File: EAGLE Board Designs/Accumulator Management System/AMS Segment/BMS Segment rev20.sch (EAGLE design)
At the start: 159 parts, among them J1 CONNECTOR-2_MICROFIT_SMD_RIGH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, J10 CONNECTOR-2_MICROFIT_SMD_RIGH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, J100 CONNECTOR-1_5222_, J101 CONNECTOR-1_5222_, J102 CONNECTOR-1_5222_, J103 CONNECTOR-1_5222_, J104 CONNECTOR-1_5222_, J105 CONNECTOR-1_5222_, J106 CONNECTOR-1_5222_, J107 CONNECTOR-1_5222_, J108 CONNECTOR-1_5222_, J109 CONNECTOR-1_5222_, J11 CONNECTOR-2_MICROFIT_SMD_RIGH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, J110 CONNECTOR-1_5222_, J111 CONNECTOR-1_5222_, J112 CONNECTOR-1_5222_, J113 CONNECTOR-1_5222_, J114 CONNECTOR-1_5222_, J115 CONNECTOR-1_5222_, J116 CONNECTOR-1_5222_, J117 CONNECTOR-1_5222_, J118 CONNECTOR-1_5222_, J119 CONNECTOR-1_5222_, J12 CONNECTOR-2_MICROFIT_SMD_RIGH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, J120 CONNECTOR-1_5222_, J121 CONNECTOR-1_5222_, J2 CONNECTOR-2_MICROFIT_SMD_RIGH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, J3 CONNECTOR-2_MICROFIT_SMD_RIGH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, J4 CONNECTOR-2_MICROFIT_SMD_RIGH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, J6 CONNECTOR-2_MICROFIT_SMD_RIGH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, J8 CONNECTOR-2_MICROFIT_SMD_RIGH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, J9 CONNECTOR-2_MICROFIT_SMD_RIGH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, T2 TRANSFORMER_HM2112ZNLT, U1 SHT31-ARP-B, U2 LTC6811-1, U3 LT3990-5, U4 LT3990-5, U5 LTC6811-1, U6 SHT31-ARP-B

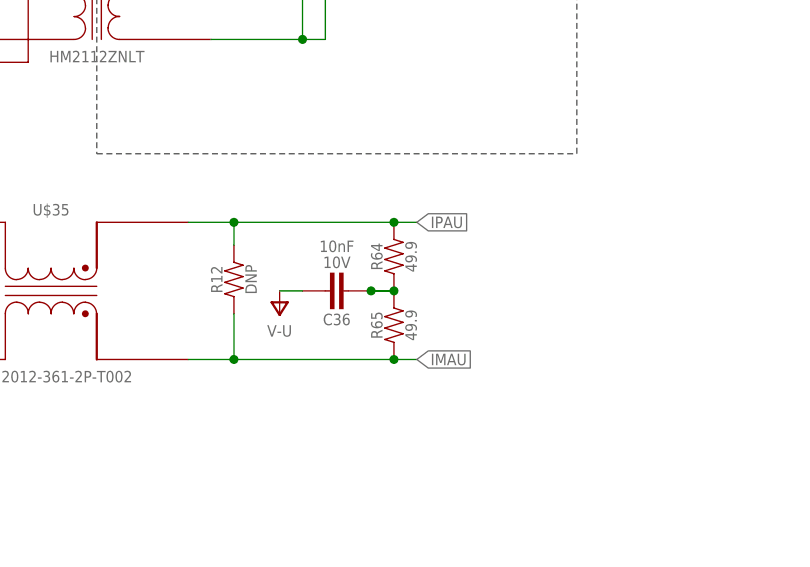
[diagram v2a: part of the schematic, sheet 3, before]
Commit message: Added Coupling Capacitors
Added Coupling Capacitors for isolation and to filter out DC noise in series for on-board chip-to-chip connection.
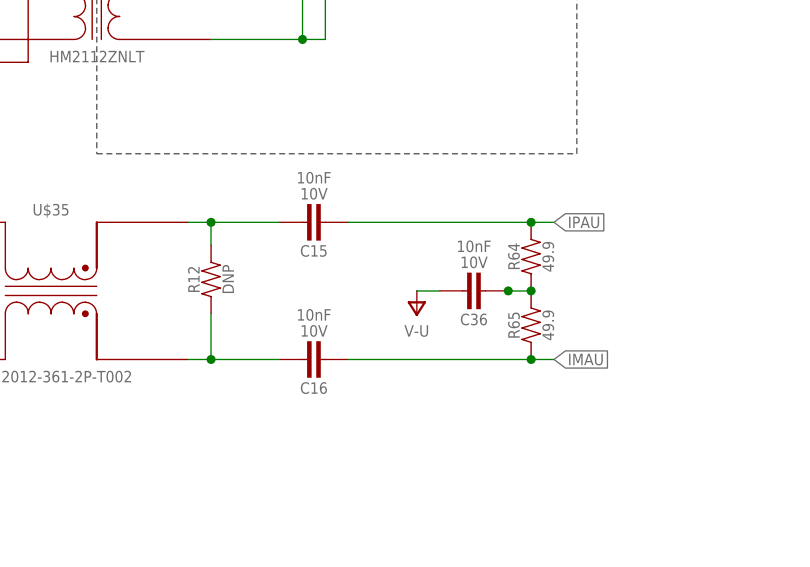
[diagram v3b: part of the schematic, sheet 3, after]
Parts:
- added C15, C16: CAPACITOR_0603_10V_10NF, HyTechDevices:CAPACITOR_0603_10V_10NF
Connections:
- net IMAU: now also C16.1, C16.2
- net IPAU: now also C15.1, C15.2
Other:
- moved on the sheet: C36, R12, R64, R65
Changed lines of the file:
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@@
 <part name="R11" library="HyTechDevices" deviceset="RESISTOR_?_*" device="0603" technology="DNP" value="RESISTOR_0603_DNP"/>
 <part name="R12" library="HyTechDevices" deviceset="RESISTOR_?_*" device="0603" technology="DNP" value="RESISTOR_0603_DNP"/>
+<part name="C15" library="HyTechDevices" deviceset="CAPACITOR_?_*" device="0603" technology="10V_10NF"/>
+<part name="C16" library="HyTechDevices" deviceset="CAPACITOR_?_*" device="0603" technology="10V_10NF"/>
 </parts>
 <sheets>
@@
 <attribute name="CAPACITANCE" x="71.882" y="138.43" size="1.27" layer="96" rot="R270" align="top-center"/>
 </instance>
-<instance part="R64" gate="G$1" x="137.16" y="83.82" smashed="yes" rot="R90">
-<attribute name="NAME" x="135.89" y="82.55" size="1.27" layer="95" rot="R90" align="bottom-center"/>
-<attribute name="RESISTANCE" x="138.43" y="82.55" size="1.27" layer="96" rot="R90" align="top-center"/>
-</instance>
-<instance part="R65" gate="G$1" x="137.16" y="76.2" smashed="yes" rot="R90">
-<attribute name="NAME" x="135.89" y="74.93" size="1.27" layer="95" rot="R90" align="bottom-center"/>
-<attribute name="RESISTANCE" x="138.43" y="74.93" size="1.27" layer="96" rot="R90" align="top-center"/>
-</instance>
-<instance part="C36" gate="G$1" x="129.54" y="78.74" smashed="yes" rot="R180">
-<attribute name="NAME" x="130.81" y="76.2" size="1.27" layer="95" rot="R180" align="bottom-center"/>
-<attribute name="VOLTAGE" x="130.81" y="81.28" size="1.27" layer="96" rot="R180" align="top-center"/>
-<attribute name="CAPACITANCE" x="130.81" y="83.058" size="1.27" layer="96" rot="R180" align="top-center"/>
+<instance part="R64" gate="G$1" x="152.4" y="83.82" smashed="yes" rot="R90">
+<attribute name="NAME" x="151.13" y="82.55" size="1.27" layer="95" rot="R90" align="bottom-center"/>
+<attribute name="RESISTANCE" x="153.67" y="82.55" size="1.27" layer="96" rot="R90" align="top-center"/>
+</instance>
+<instance part="R65" gate="G$1" x="152.4" y="76.2" smashed="yes" rot="R90">
+<attribute name="NAME" x="151.13" y="74.93" size="1.27" layer="95" rot="R90" align="bottom-center"/>
+<attribute name="RESISTANCE" x="153.67" y="74.93" size="1.27" layer="96" rot="R90" align="top-center"/>
+</instance>
+<instance part="C36" gate="G$1" x="144.78" y="78.74" smashed="yes" rot="R180">
+<attribute name="NAME" x="146.05" y="76.2" size="1.27" layer="95" rot="R180" align="bottom-center"/>
+<attribute name="VOLTAGE" x="146.05" y="81.28" size="1.27" layer="96" rot="R180" align="top-center"/>
+<attribute name="CAPACITANCE" x="146.05" y="83.058" size="1.27" layer="96" rot="R180" align="top-center"/>
 </instance>
 <instance part="P100" gate="G$1" x="81.28" y="132.08" smashed="yes">
 <attribute name="VALUE" x="81.28" y="130.81" size="1.27" layer="96" align="top-center"/>
 </instance>
-<instance part="P101" gate="G$1" x="124.46" y="76.2" smashed="yes">
-<attribute name="VALUE" x="124.46" y="74.93" size="1.27" layer="96" align="top-center"/>
+<instance part="P101" gate="G$1" x="139.7" y="76.2" smashed="yes">
+<attribute name="VALUE" x="139.7" y="74.93" size="1.27" layer="96" align="top-center"/>
 </instance>
 <instance part="R69" gate="G$1" x="127" y="119.38" smashed="yes" rot="R90">
@@
 <attribute name="RESISTANCE" x="82.55" y="80.01" size="1.27" layer="96" rot="R90" align="top-center"/>
 </instance>
-<instance part="R12" gate="G$1" x="119.38" y="81.28" smashed="yes" rot="R90">
-<attribute name="NAME" x="118.11" y="80.01" size="1.27" layer="95" rot="R90" align="bottom-center"/>
-<attribute name="RESISTANCE" x="120.65" y="80.01" size="1.27" layer="96" rot="R90" align="top-center"/>
+<instance part="R12" gate="G$1" x="116.84" y="81.28" smashed="yes" rot="R90">
+<attribute name="NAME" x="115.57" y="80.01" size="1.27" layer="95" rot="R90" align="bottom-center"/>
+<attribute name="RESISTANCE" x="118.11" y="80.01" size="1.27" layer="96" rot="R90" align="top-center"/>
+</instance>
+<instance part="C15" gate="G$1" x="127" y="86.36" smashed="yes" rot="R180">
+<attribute name="NAME" x="128.27" y="83.82" size="1.27" layer="95" rot="R180" align="bottom-center"/>
+<attribute name="VOLTAGE" x="128.27" y="88.9" size="1.27" layer="96" rot="R180" align="top-center"/>
+<attribute name="CAPACITANCE" x="128.27" y="90.678" size="1.27" layer="96" rot="R180" align="top-center"/>
+</instance>
+<instance part="C16" gate="G$1" x="127" y="71.12" smashed="yes" rot="R180">
+<attribute name="NAME" x="128.27" y="68.58" size="1.27" layer="95" rot="R180" align="bottom-center"/>
+<attribute name="VOLTAGE" x="128.27" y="73.66" size="1.27" layer="96" rot="R180" align="top-center"/>
+<attribute name="CAPACITANCE" x="128.27" y="75.438" size="1.27" layer="96" rot="R180" align="top-center"/>
 </instance>
 </instances>
@@
 <net name="IMAU" class="5">
 <segment>
-<pinref part="R65" gate="G$1" pin="1"/>
-<wire x1="137.16" y1="71.12" x2="139.7" y2="71.12" width="0.1524" layer="91"/>
-<label x="139.7" y="71.12" size="1.27" layer="95" xref="yes"/>
 <pinref part="U$35" gate="G$1" pin="3"/>
-<wire x1="137.16" y1="71.12" x2="119.38" y2="71.12" width="0.1524" layer="91"/>
-<junction x="137.16" y="71.12"/>
 <pinref part="R12" gate="G$1" pin="1"/>
-<wire x1="119.38" y1="71.12" x2="114.3" y2="71.12" width="0.1524" layer="91"/>
-<wire x1="119.38" y1="76.2" x2="119.38" y2="71.12" width="0.1524" layer="91"/>
-<junction x="119.38" y="71.12"/>
+<wire x1="116.84" y1="71.12" x2="114.3" y2="71.12" width="0.1524" layer="91"/>
+<wire x1="116.84" y1="76.2" x2="116.84" y2="71.12" width="0.1524" layer="91"/>
+<pinref part="C16" gate="G$1" pin="1"/>
+<wire x1="124.46" y1="71.12" x2="116.84" y2="71.12" width="0.1524" layer="91"/>
+<junction x="116.84" y="71.12"/>
+</segment>
+<segment>
+<pinref part="R65" gate="G$1" pin="1"/>
+<wire x1="152.4" y1="71.12" x2="154.94" y2="71.12" width="0.1524" layer="91"/>
+<label x="154.94" y="71.12" size="1.27" layer="95" xref="yes"/>
+<pinref part="C16" gate="G$1" pin="2"/>
+<wire x1="152.4" y1="71.12" x2="132.08" y2="71.12" width="0.1524" layer="91"/>
+<junction x="152.4" y="71.12"/>
 </segment>
 </net>
 <net name="IPAU" class="5">
 <segment>
-<pinref part="R64" gate="G$1" pin="2"/>
-<wire x1="137.16" y1="86.36" x2="139.7" y2="86.36" width="0.1524" layer="91"/>
-<label x="139.7" y="86.36" size="1.27" layer="95" xref="yes"/>
 <pinref part="U$35" gate="G$1" pin="4"/>
-<wire x1="137.16" y1="86.36" x2="119.38" y2="86.36" width="0.1524" layer="91"/>
-<junction x="137.16" y="86.36"/>
 <pinref part="R12" gate="G$1" pin="2"/>
-<wire x1="119.38" y1="86.36" x2="114.3" y2="86.36" width="0.1524" layer="91"/>
-<wire x1="119.38" y1="83.82" x2="119.38" y2="86.36" width="0.1524" layer="91"/>
-<junction x="119.38" y="86.36"/>
+<wire x1="116.84" y1="86.36" x2="114.3" y2="86.36" width="0.1524" layer="91"/>
+<wire x1="116.84" y1="83.82" x2="116.84" y2="86.36" width="0.1524" layer="91"/>
+<pinref part="C15" gate="G$1" pin="1"/>
+<wire x1="124.46" y1="86.36" x2="116.84" y2="86.36" width="0.1524" layer="91"/>
+<junction x="116.84" y="86.36"/>
+</segment>
+<segment>
+<pinref part="R64" gate="G$1" pin="2"/>
+<wire x1="152.4" y1="86.36" x2="154.94" y2="86.36" width="0.1524" layer="91"/>
+<label x="154.94" y="86.36" size="1.27" layer="95" xref="yes"/>
+<pinref part="C15" gate="G$1" pin="2"/>
+<wire x1="152.4" y1="86.36" x2="132.08" y2="86.36" width="0.1524" layer="91"/>
+<junction x="152.4" y="86.36"/>
 </segment>
 </net>
@@
 <pinref part="R65" gate="G$1" pin="2"/>
 <pinref part="C36" gate="G$1" pin="2"/>
-<wire x1="134.62" y1="78.74" x2="137.16" y2="78.74" width="0.1524" layer="91"/>
-<junction x="137.16" y="78.74"/>
-<wire x1="134.62" y1="78.74" x2="137.16" y2="78.74" width="0.1524" layer="91"/>
-<junction x="134.62" y="78.74"/>
+<junction x="152.4" y="78.74"/>
+<wire x1="149.86" y1="78.74" x2="152.4" y2="78.74" width="0.1524" layer="91"/>
+<junction x="149.86" y="78.74"/>
 </segment>
 </net>
@@
 <segment>
 <pinref part="C36" gate="G$1" pin="1"/>
-<wire x1="127" y1="78.74" x2="124.46" y2="78.74" width="0.1524" layer="91"/>
+<wire x1="142.24" y1="78.74" x2="139.7" y2="78.74" width="0.1524" layer="91"/>
 <pinref part="P101" gate="G$1" pin="V-U"/>
 </segment>

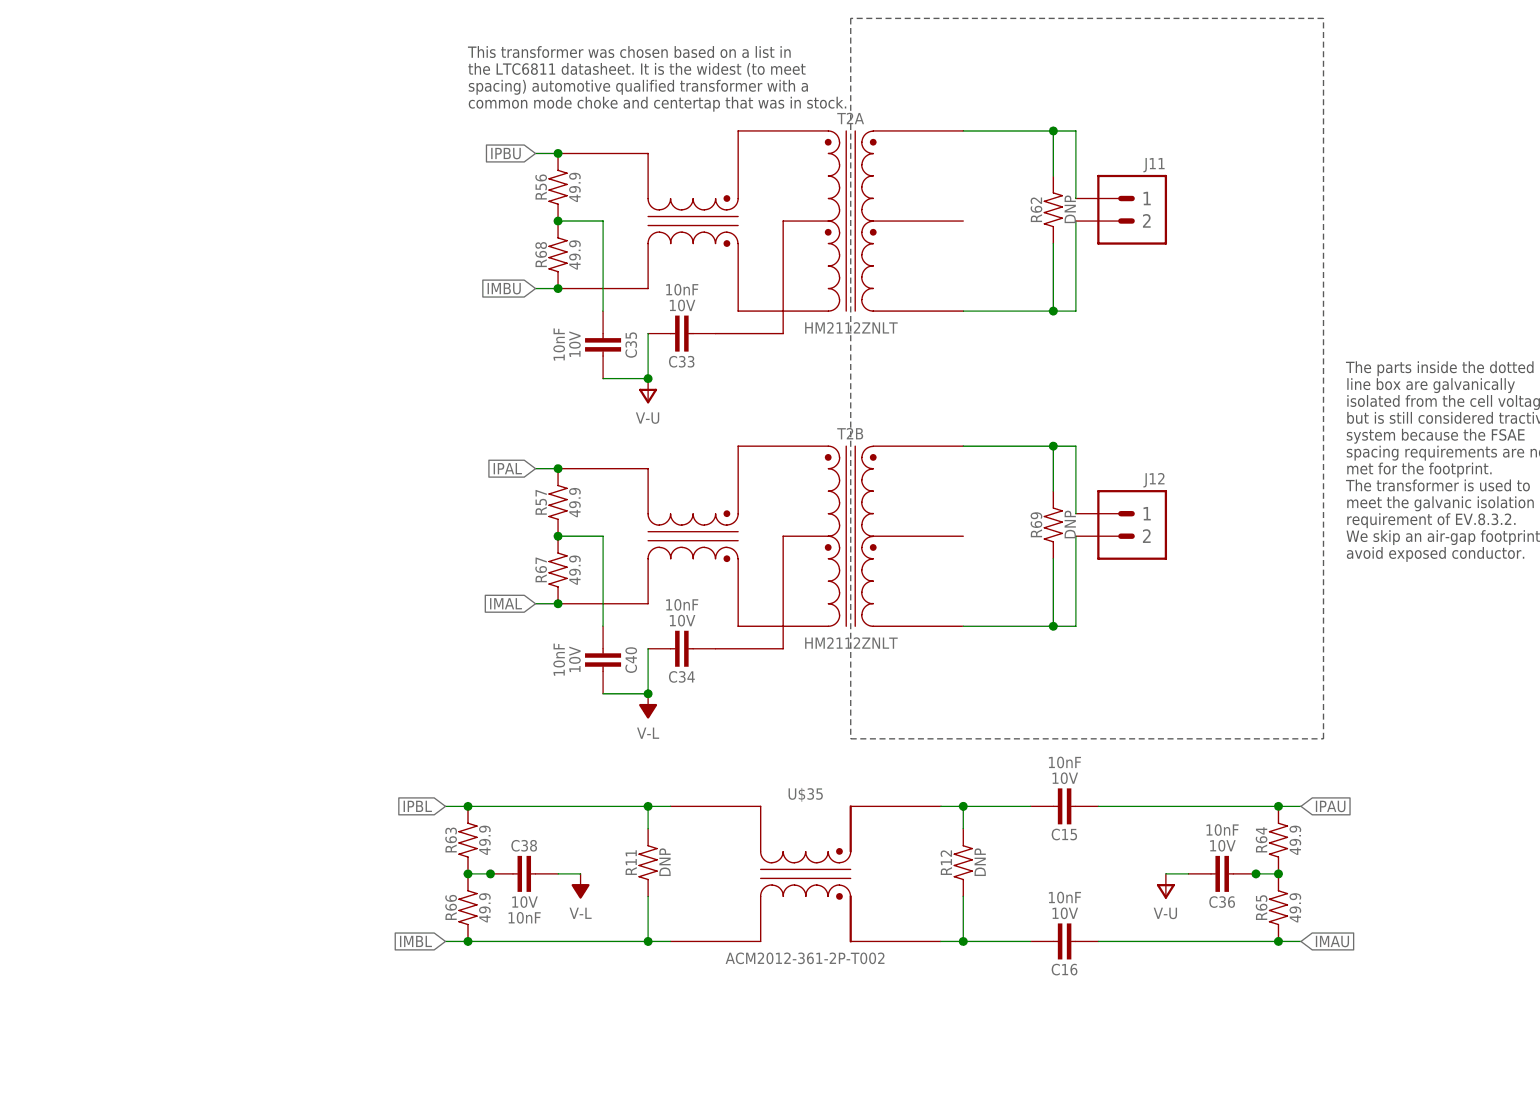
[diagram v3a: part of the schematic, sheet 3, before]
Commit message: Initial rev20 Board Routing
Initial routing for BMS rev20 board.
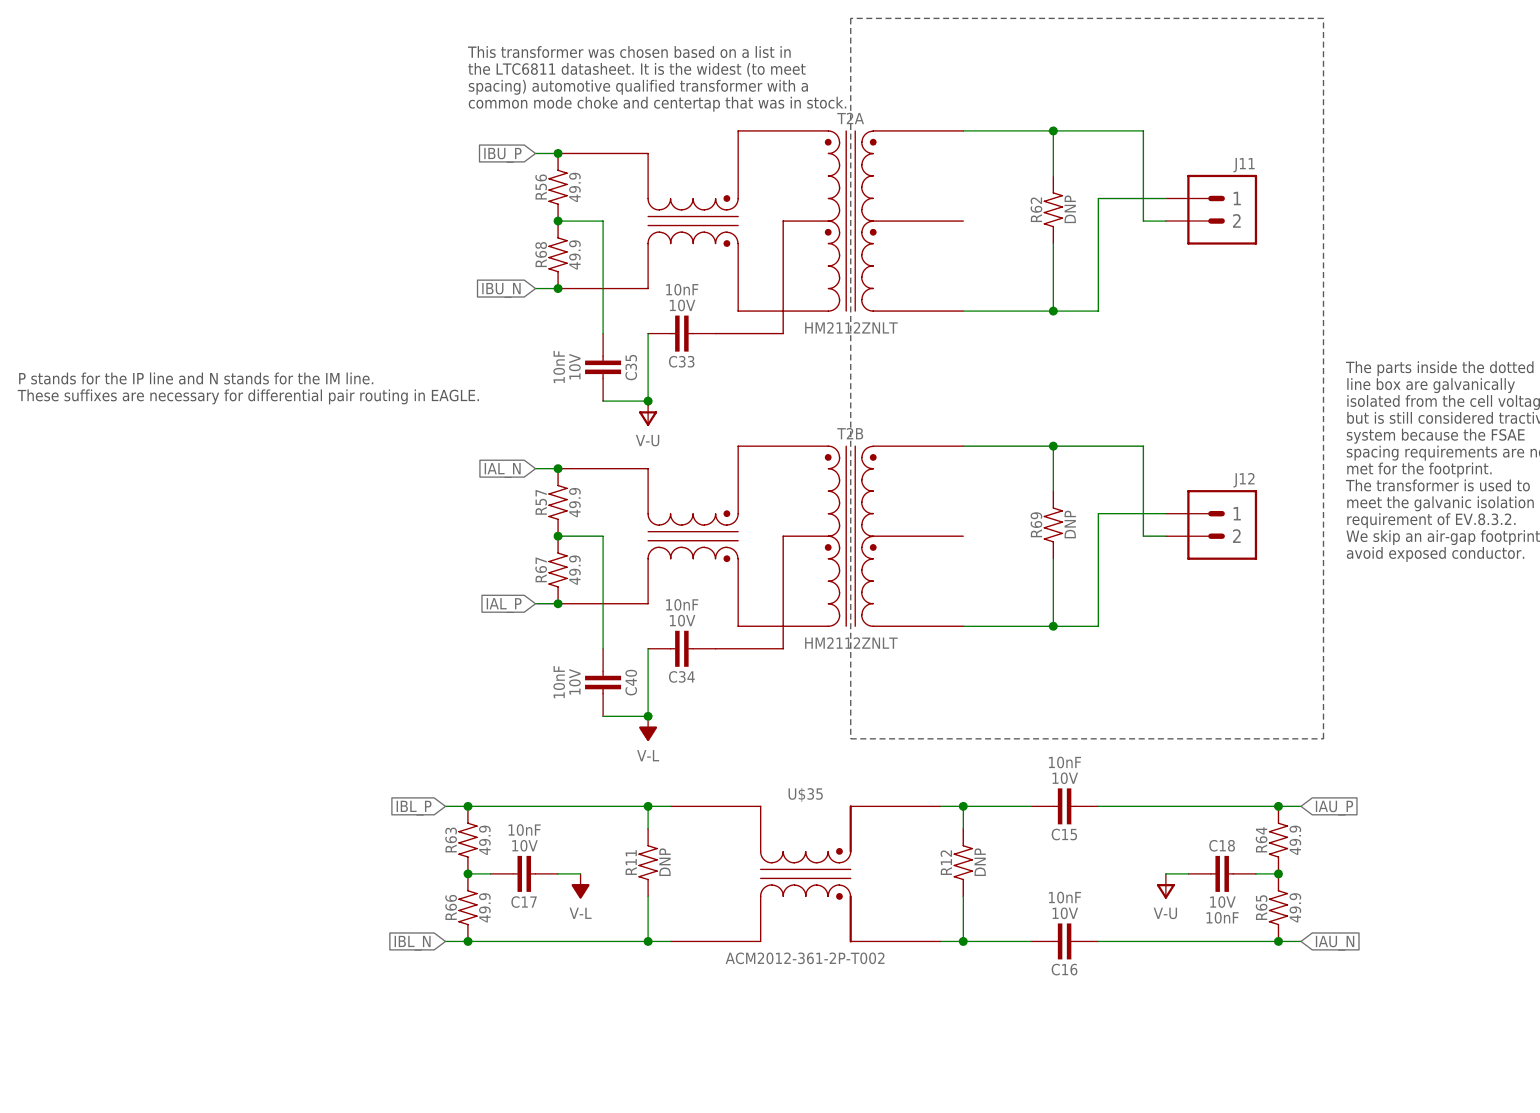
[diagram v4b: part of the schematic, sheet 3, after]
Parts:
- removed C36, C38: CAPACITOR_0603_10V_10NF, HyTechDevices:CAPACITOR_0603_10V_10NF
- added C17, C18: CAPACITOR_0603_10V_10NF, HyTechDevices:CAPACITOR_0603_10V_10NF
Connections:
- net IMAL renamed IAL_P
- net IMBL renamed IBL_N
- net IMBU renamed IBU_N
- net IPAL renamed IAL_N
- net IPBL renamed IBL_P
- net IPBU renamed IBU_P
- net N$14 renamed SHUNT_H_OUT
- net N$15 renamed SHUNT_L_IN
- removed net IMAU: C16.1, C16.2, R12.1, R65.1, U$35.3, U5.IMA
- removed net IPAU: C15.1, C15.2, R12.2, R64.2, U$35.4, U5.IPA
- removed net N$21: J12.2, R69.1, T2B.MX-
- removed net N$23: J12.1, R69.2, T2B.MX+
- removed net N$24: C38.2, R63.1, R66.2
- removed net N$28: J11.1, R62.2, T2A.MX+
- removed net N$31: J11.2, R62.1, T2A.MX-
- removed net N$35: C36.2, R64.1, R65.2
- removed net V-L1: C34.1, C40.1
- new net IAU_N: C16.2, R65.1, U5.IMA
- new net IAU_N_CHOKED: C16.1, R12.1, U$35.3
- new net IAU_P: C15.2, R64.2, U5.IPA
- new net IAU_P_CHOKED: C15.1, R12.2, U$35.4
- new net IIN_N: J12.2, R69.2, T2B.MX+
- new net IIN_P: J12.1, R69.1, T2B.MX-
- new net IOUT_N: J11.1, R62.1, T2A.MX-
- new net IOUT_P: J11.2, R62.2, T2A.MX+
- new net SHUNT_H_IN: C17.1, R63.1, R66.2
- new net SHUNT_L_OUT: C18.1, R64.1, R65.2
- net N$13: now also R43.1
- net N$8: now also R16.1
- net V-L: now also C17.2, C34.1, C40.1; no longer C38.1, R16.1
- net V-U: now also C18.2; no longer C36.1, R43.1
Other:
- note added: "P stands for the IP line and N stands for the IM line. These suffixes are necessary for differential pair routing in EAGLE."
- moved on the sheet: C35, C40, J11, J12, R16, R17, R42, R43
